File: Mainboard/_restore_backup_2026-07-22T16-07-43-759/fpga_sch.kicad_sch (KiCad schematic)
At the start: 12 parts, among them IC6 XC7S50-L1CSGA324I, J4 Left Daughter Connector, J5 Right Daughter Connector, J6 CART, J7 Cart SW, J9 Screen zif FFC/FPC

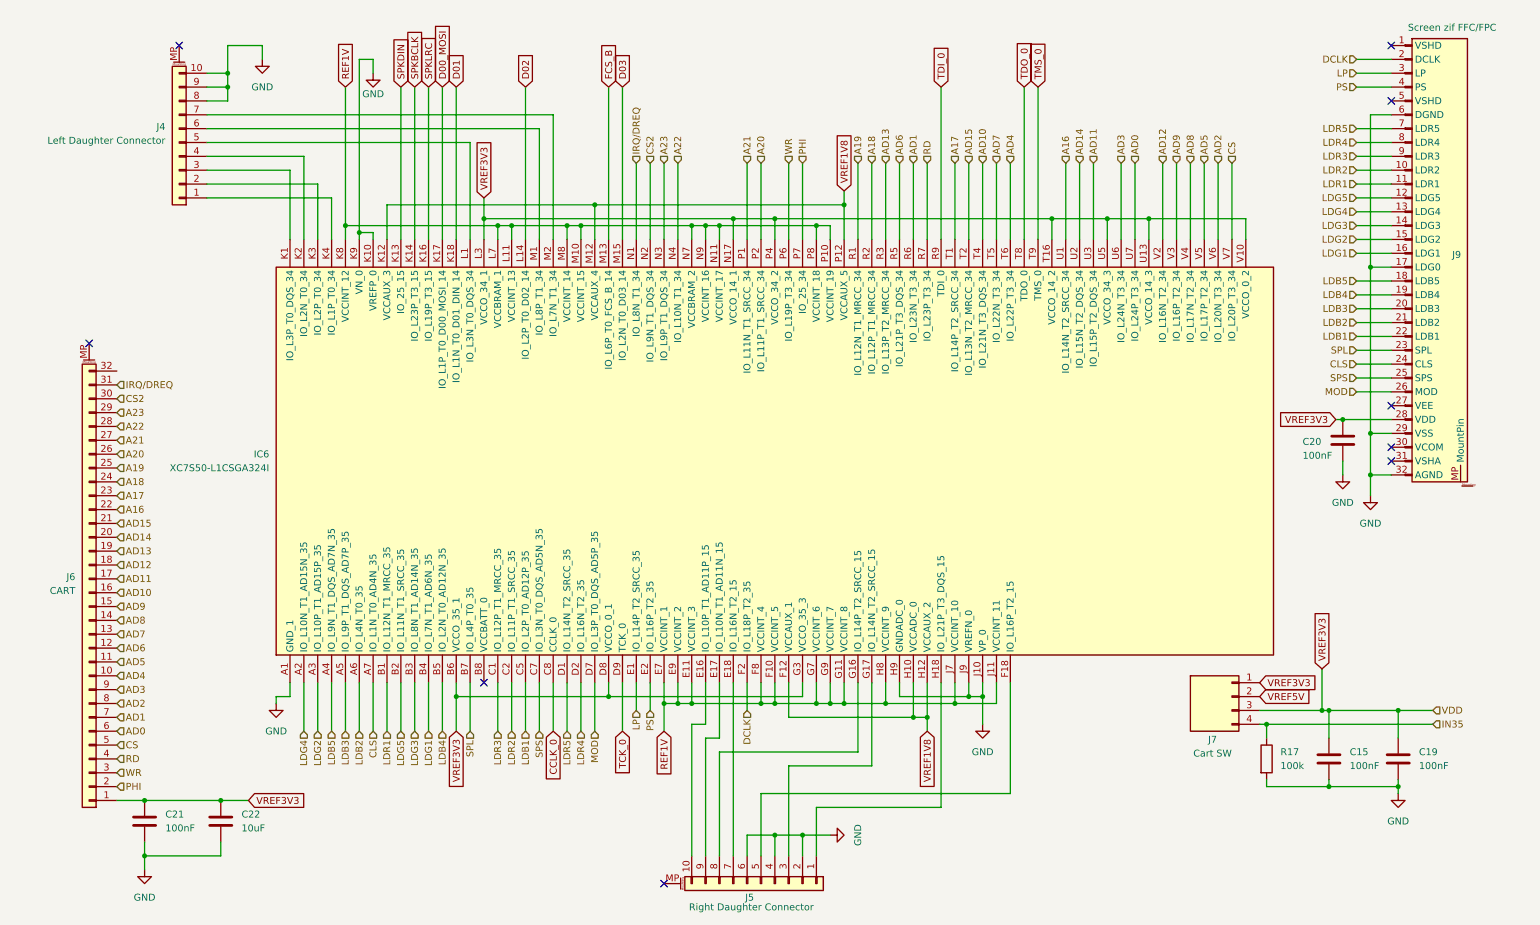
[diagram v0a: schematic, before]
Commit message: + Power sw, + R arrays, sync PCB/schem
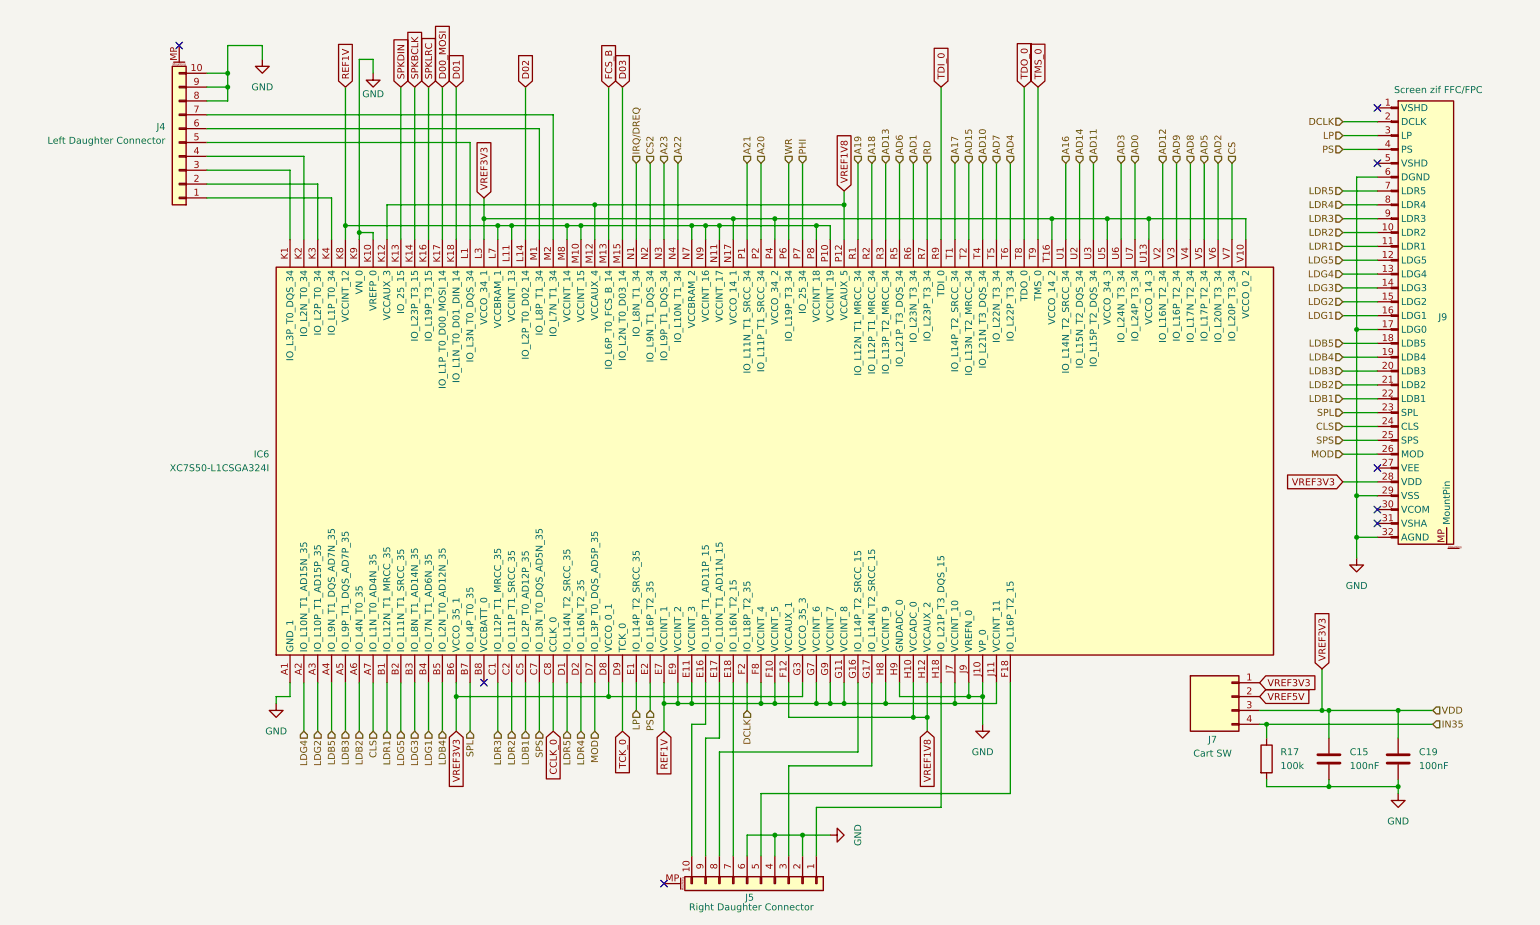
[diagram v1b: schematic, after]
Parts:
- removed C20: 100nF, Capacitor_SMD:C_0402_1005Metric, symbol Device:C
- removed C21: 100nF, Capacitor_SMD:C_0603_1608Metric, symbol Device:C
- removed C22: 10uF, Capacitor_SMD:C_0603_1608Metric, symbol Device:C
- removed J6: CART, AGBRE:AGB Cart Pin, symbol Connector_Generic_MountingPin:Conn_01x32_MountingPin
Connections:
- no-connect marks 9 -> 8
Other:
- moved on the sheet: J9
